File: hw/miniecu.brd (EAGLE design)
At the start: 50 x 50 mm, 60 parts

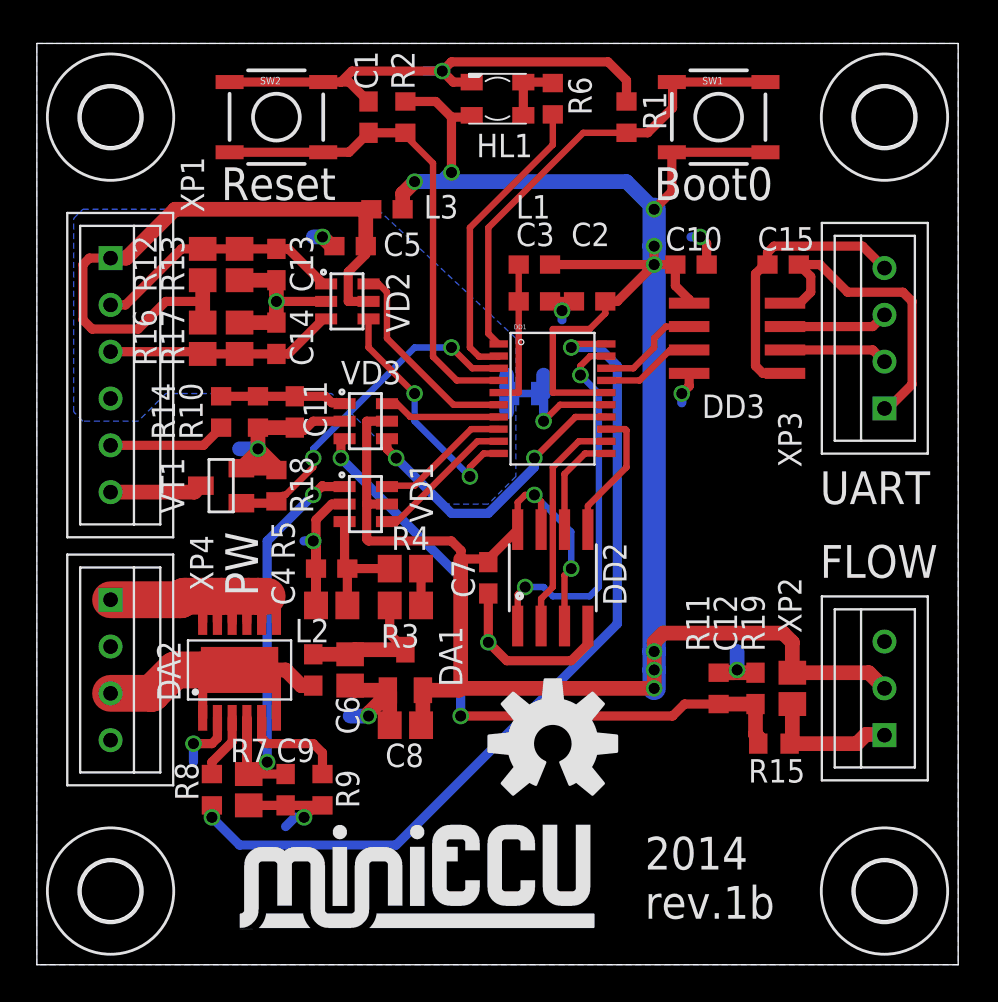
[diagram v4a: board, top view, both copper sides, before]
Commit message: hw: release v1c & update gerbers
changes from v1b:

- Use rounded corners.
- Add one GND drill.
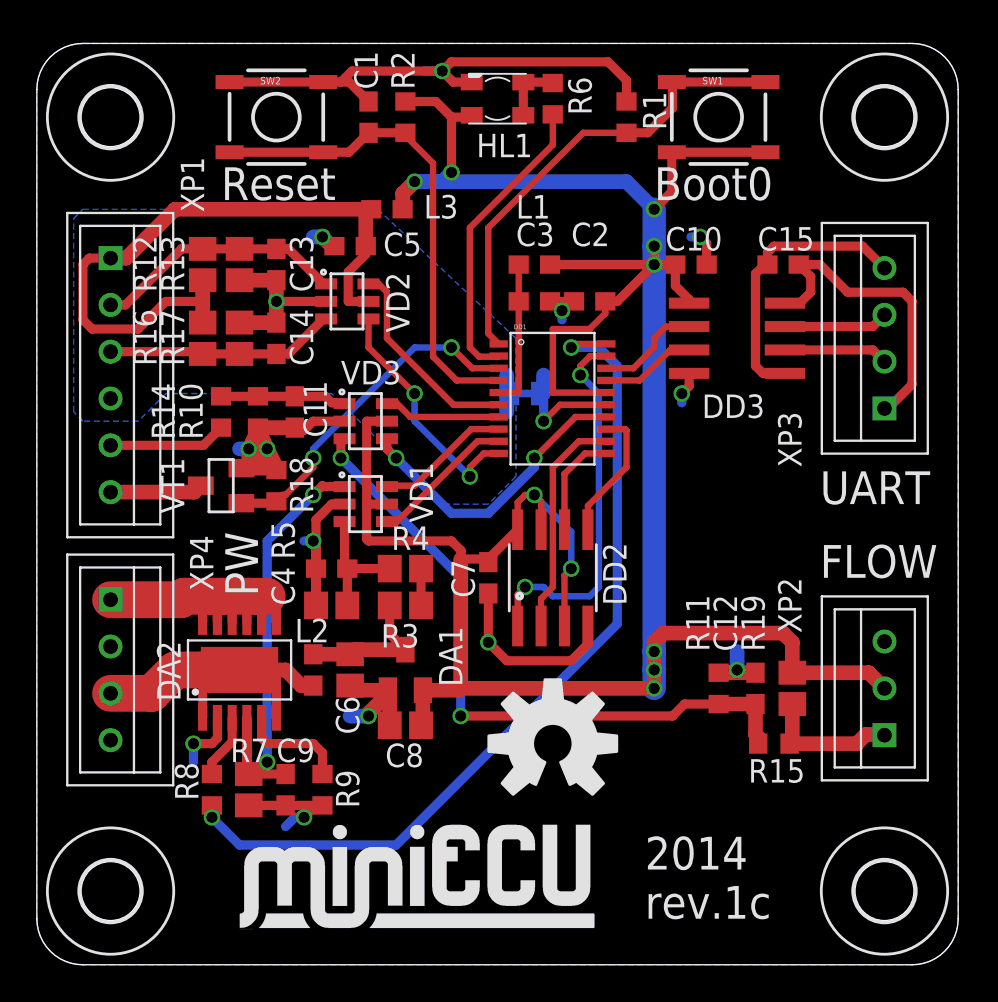
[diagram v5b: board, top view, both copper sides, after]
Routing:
- net GND: track 94.8 -> 98.6 mm, vias 12 -> 13
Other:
- outline, holes or cut-outs redrawn
- board text added: "2014 rev.1c"
- board text added: "miniECU rev.1c engine monitoring with kill switch"
- board text removed: "2014 rev.1b"
- board text removed: "miniECU rev.1b engine monitoring with kill switch"
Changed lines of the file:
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@@
 <board>
 <plain>
-<wire x1="0" y1="0" x2="50" y2="0" width="0" layer="20"/>
-<wire x1="50" y1="0" x2="50" y2="50" width="0" layer="20"/>
-<wire x1="50" y1="50" x2="0" y2="50" width="0" layer="20"/>
-<wire x1="0" y1="50" x2="0" y2="0" width="0" layer="20"/>
+<wire x1="0" y1="2.5" x2="2.5" y2="0" width="0" layer="20" curve="90"/>
+<wire x1="2.5" y1="0" x2="47.5" y2="0" width="0" layer="20"/>
+<wire x1="47.5" y1="0" x2="50" y2="2.5" width="0" layer="20" curve="90"/>
+<wire x1="50" y1="2.5" x2="50" y2="47.5" width="0" layer="20"/>
+<wire x1="50" y1="47.5" x2="47.5" y2="50" width="0" layer="20" curve="90"/>
+<wire x1="47.5" y1="50" x2="2.5" y2="50" width="0" layer="20"/>
+<wire x1="2.5" y1="50" x2="0" y2="47.5" width="0" layer="20" curve="90"/>
+<wire x1="0" y1="47.5" x2="0" y2="2.5" width="0" layer="20"/>
 <polygon width="0.5" layer="42">
 <vertex x="50" y="28"/>
@@
 </polygon>
 <text x="33" y="2.5" size="1.778" layer="21" font="vector">2014
-rev.1b</text>
+rev.1c</text>
 <text x="42.5" y="25" size="1.778" layer="21" font="vector">UART</text>
 <text x="42.5" y="21" size="1.778" layer="21" font="vector">FLOW</text>
@@
 <text x="35" y="31.75" size="2" layer="22" font="vector" rot="MR0" align="bottom-right">TXD</text>
 <text x="35" y="29.25" size="2" layer="22" font="vector" rot="MR0" align="bottom-right">VCCi</text>
-<text x="10.5" y="9.5" size="2" layer="22" font="fixed" rot="MR180">miniECU rev.1b
+<text x="10.5" y="9.5" size="2" layer="22" font="fixed" rot="MR180">miniECU rev.1c
 engine monitoring
 with kill switch</text>
@@
 <contactref element="HL1" pad="1"/>
 <polygon width="0.5" layer="16" isolate="0.254" rank="2">
-<vertex x="0" y="50"/>
-<vertex x="50" y="50"/>
-<vertex x="50" y="0"/>
-<vertex x="0" y="0"/>
+<vertex x="2.5" y="50"/>
+<vertex x="47.5" y="50" curve="-90"/>
+<vertex x="50" y="47.5"/>
+<vertex x="50" y="2.5" curve="-90"/>
+<vertex x="47.5" y="0"/>
+<vertex x="2.5" y="0" curve="-90"/>
+<vertex x="0" y="2.5"/>
+<vertex x="0" y="47.5" curve="-90"/>
 </polygon>
 <contactref element="R1" pad="1"/>
 <contactref element="SW2" pad="1"/>
 <wire x1="14.15" y1="29" x2="14" y2="29.15" width="0.5" layer="1"/>
-<wire x1="12" y1="29.15" x2="12" y2="28" width="0.8" layer="1"/>
-<wire x1="12" y1="28" x2="12" y2="27.85" width="0.8" layer="1"/>
-<wire x1="12" y1="27.85" x2="11.1" y2="26.95" width="0.8" layer="1"/>
+<wire x1="12" y1="29.15" x2="12.5" y2="28" width="0.8" layer="1"/>
 <wire x1="11.1" y1="26.95" x2="12.9" y2="26.95" width="0.8" layer="1"/>
 <wire x1="12.9" y1="26.95" x2="13" y2="26.85" width="0.8" layer="1"/>
 <wire x1="12" y1="29.15" x2="14" y2="29.15" width="0.8" layer="1"/>
 <wire x1="13" y1="26.85" x2="13" y2="27" width="0.8" layer="1"/>
-<wire x1="13" y1="27" x2="12" y2="28" width="0.8" layer="1"/>
-<via x="12" y="28" extent="1-16" drill="0.6"/>
-<wire x1="12" y1="28" x2="11" y2="28" width="0.8" layer="16"/>
+<wire x1="13" y1="27" x2="12.5" y2="28" width="0.8" layer="1"/>
+<via x="12.5" y="28" extent="1-16" drill="0.6"/>
+<wire x1="12.5" y1="28" x2="11" y2="28" width="0.8" layer="16"/>
 <wire x1="19.15" y1="13" x2="19.15" y2="14.8" width="0.8" layer="1"/>
 <wire x1="19.15" y1="14.8" x2="19.05" y2="14.9" width="0.8" layer="1"/>
@@
 <wire x1="27.5" y1="30.635" x2="27.135" y2="31" width="0.5" layer="16"/>
 <wire x1="27.5" y1="31" x2="27.5" y2="32" width="0.8" layer="16"/>
+<via x="11.5" y="28" extent="1-16" drill="0.6"/>
+<wire x1="11.5" y1="28" x2="11.5" y2="27" width="0.8" layer="1"/>
+<wire x1="11.5" y1="28" x2="12" y2="29" width="0.8" layer="1"/>
+<wire x1="11.5" y1="28" x2="12.5" y2="28" width="0.8" layer="1"/>
+<wire x1="11.5" y1="28" x2="13" y2="27" width="0.8" layer="1"/>
 <wire x1="27.135" y1="31" x2="27.5" y2="31" width="0" layer="19" extent="16-16"/>
 </signal>

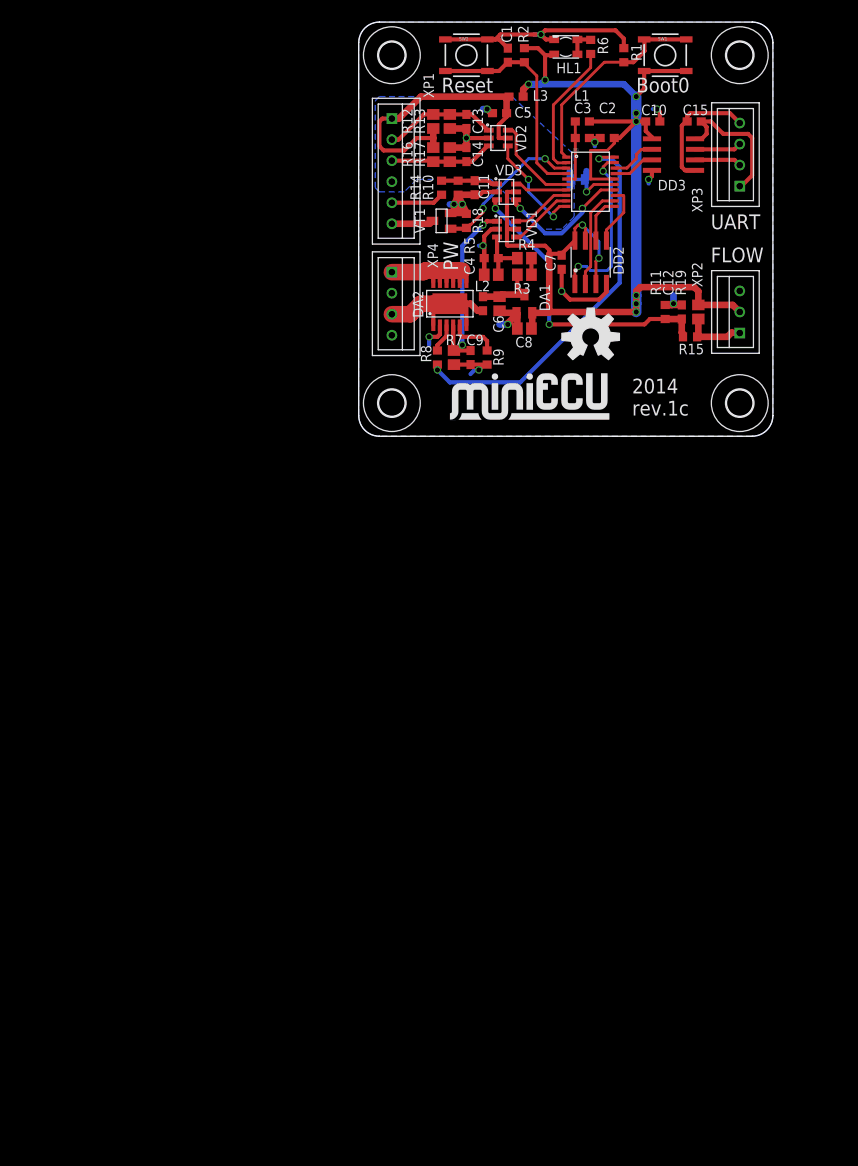
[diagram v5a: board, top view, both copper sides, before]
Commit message: hw: replace mcu
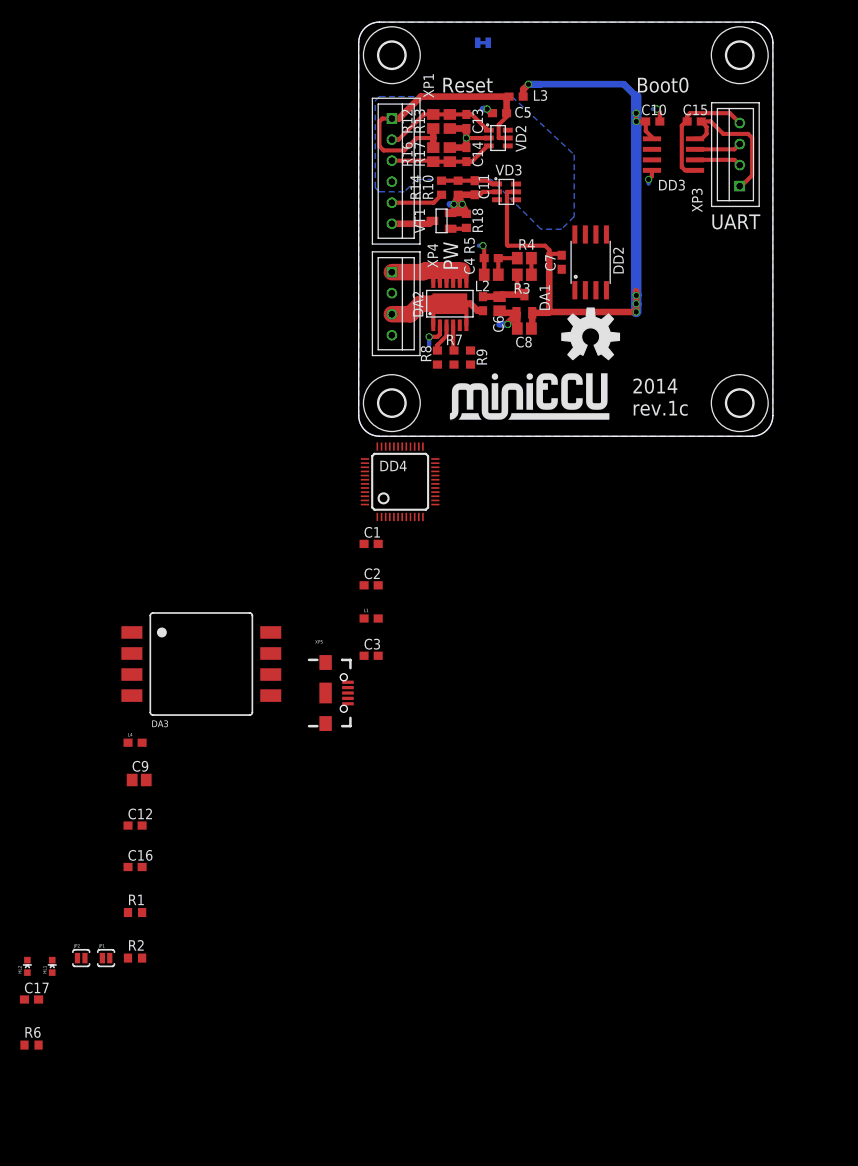
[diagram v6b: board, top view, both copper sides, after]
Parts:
- removed DD1: STM32F050F, stm32f050:TSSOP20
- removed R11: np, resistor:R0603
- removed R15: 140, resistor:R0603
- removed R19: 10k 1%, resistor:R0805
- removed SW1, SW2: (no value), SparkFun-Electromechanical:TACTILE_SWITCH_SMD
- removed VD1: USBLC6-2L, usblc6:SOT-23-6L
- removed XP2: B3B-XH-A, miniecu-con:B3B-XH
- added C16: 0.33, resistor:C0603
- added C17: 0.1, resistor:C0603
- added DA3: MP3V5004DP, microbuilder:SOP8-1351
- added DD4: STM32F373C, stm32f373:LQFP48
- added HL2: RED, SparkFun-LED:LED-0603
- added JP1, JP2: (no value), SparkFun-Passives:SJ_2S-NO
- added L4: FB, SparkFun-Passives:0603
- added XP5: USB_MICROB_PLUGCONN-11752, SparkFun-Connectors:USB-B-MICRO-SMD_V03
- C1: value 0.022 -> 0.1
- C12: value 0.022 -> 0.01
- C9: value 0.1 -> 1.0; device resistor:C0603 -> resistor:C0805
- DD2: value SPI_FLASH-X25XXSMD -> SPI_FLASH-X25XXSMD1; device SparkFun-DigitalIC:SO08 -> SparkFun-DigitalIC:SO08-EIAJ
- HL1: value KAA-3528ESGC -> GREEN; device led2:KA-3528 -> SparkFun-LED:LED-0603
- R1: value 5.1k -> 750
- R10: value np -> 10k
- R14, R6: value 140 -> 10k
- R18, R2, R9: value 5.1k -> 10k
- R7: value 10k 1% -> 1k; device resistor:R0805 -> resistor:R0603
- moved R6 138.1 mm to (-39.5, -73.5), turned to 0 degrees
- moved HL1 127.1 mm to (-37.0, -64.0), turned to 0 degrees
- moved R1 119.1 mm to (-27.0, -57.5), turned to 0 degrees
- moved R2 118.7 mm to (-27.0, -63.0), turned to 0 degrees
- moved C12 90.6 mm to (-27.0, -47.0), turned to 0 degrees
- moved C3 67.5 mm to (1.50, -26.5)
- moved L1 65.2 mm to (1.50, -22.0)
- moved C9 64.8 mm to (-26.5, -41.5), turned to 0 degrees
- moved C1 61.3 mm to (1.50, -13.0), turned to 0 degrees
- moved C2 61.1 mm to (1.50, -18.0), turned to 0 degrees
- moved PT1 20.1 mm to (15.0, 47.5)
- moved R9 2.00 mm to (13.5, 9.50)
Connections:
- removed net !NRST: C1.1, DD1.4, R2.1, SW2.3, SW2.4
- removed net AVCC: C3.1, DD1.5, L1.1
- removed net BOOT0: DD1.1, R1.2, SW1.1, SW1.2
- removed net FLOW_PULSE: C12.1, DD1.14, R11.2, R15.1, VD3.3, VD3.4
- removed net I_SENSE: C9.1, DA2.4, DD1.8, R7.1, VD1.1, VD1.6
- removed net LED: DD1.2, R6.1
- new net BAT: DD4.1
- new net FLOW: C16.1, R1.1
- new net N$10: C17.1, DD4.7, JP2.2
- new net N$11: DD4.44, JP1.1, R6.2
- new net N$3: C12.1, C9.1, DA3.2, L4.1
- new net N$5: C2.1, DD4.24, DD4.25, DD4.9, L1.1
- new net USB_DM: XP5.D-1
- new net USB_DP: XP5.D+1
- new net USB_VBUS: XP5.VBUS1
- net +3V3: now also C1.1, C3.1, DD4.17, DD4.48, JP1.2, L4.2; no longer C2.1, DD1.16, HL1.4, R19.2, R2.2, SW1.3, SW1.4, VD1.5, XP2.2
- net AGND: now also C2.2, DD4.23, DD4.8
- net FLASH_CS: no longer DD1.19
- net GND: now also C16.2, C17.2, DA3.3, DD4.47, JP2.1, R2.1, R6.1, XP5.GND1; no longer C2.2, DD1.15, HL1.1, R1.1, R11.1, SW2.1, SW2.2, VD1.2, XP2.3
- net IGN_EN: no longer DD1.20
- net MISO: no longer DD1.12
- net MOSI: no longer DD1.13
- net N$2: now also DA2.4, R7.1; no longer HL1.2, HL1.3, R6.2
- net N$4: now also DA3.4, R1.2; no longer R15.2, R19.1, XP2.1
- net OIL_PRES: no longer DD1.10
- net RPM_IN: now also R2.2; no longer DD1.7
- net RXD: no longer DD1.18
- net SCK: no longer DD1.11
- net STARTER: no longer DD1.3
- net THERM: no longer DD1.6
- net TXD: no longer DD1.17
- net V_SENSE: now also VD3.3, VD3.4; no longer DD1.9, VD1.3, VD1.4
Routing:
- net +3V3: track 153.1 -> 87.2 mm, vias 10 -> 6
- net GND: track 98.6 -> 36.4 mm, vias 13 -> 7
- net FLOW_PULSE: track 52.7 -> 0.00 mm, vias 4 -> 0
- net IGN_EN: track 47.1 -> 0.00 mm, vias 2 -> 0
- net I_SENSE: track 34.1 -> 0.00 mm, vias 2 -> 0
- net !NRST: track 26.8 -> 0.00 mm
- net BOOT0: track 25.7 -> 0.00 mm
- net FLASH_CS: track 20.7 -> 0.00 mm, vias 2 -> 0
- net STARTER: track 18.5 -> 1.94 mm, vias 2 -> 0
- net LED: track 16.3 -> 0.00 mm
- net OIL_PRES: track 25.7 -> 12.5 mm, vias 2 -> 0
- net MISO: track 12.4 -> 0.00 mm
- net THERM: track 25.0 -> 13.7 mm
- net V_SENSE: track 14.8 -> 4.51 mm
- net AVCC: track 8.04 -> 0.00 mm
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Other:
- board text removed: "+3.3"
- board text removed: "FLOW"
- board text removed: "GND"
- board text removed: "PULSE"

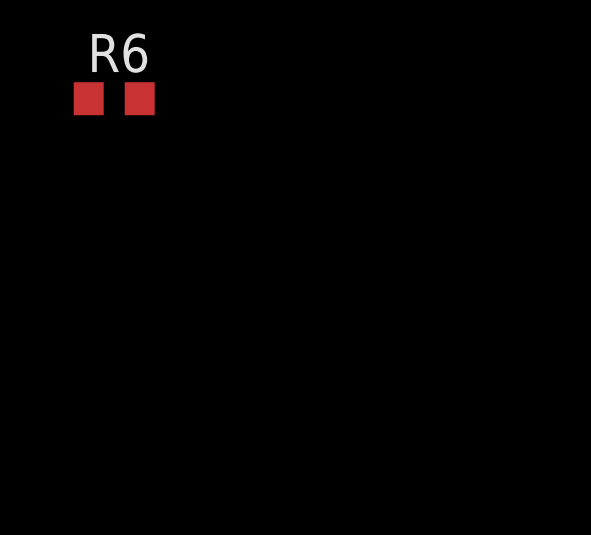
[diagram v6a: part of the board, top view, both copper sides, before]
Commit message: hw: add library for Murata CSTCE resonators
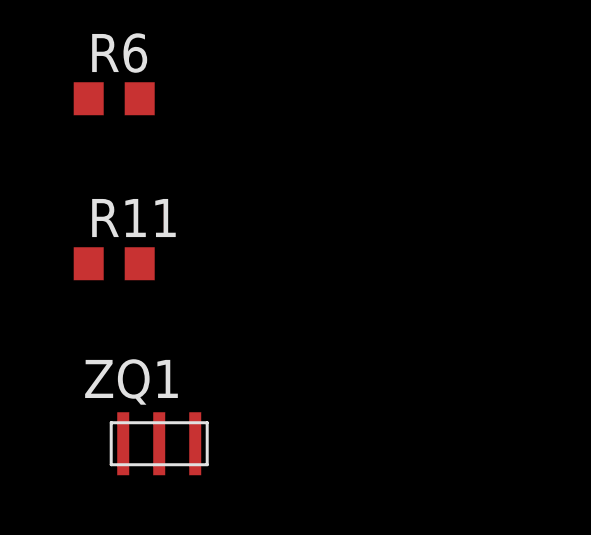
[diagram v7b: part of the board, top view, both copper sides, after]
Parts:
- added R11: 1.5k, resistor:R0603
- added ZQ1: CSTCE8M00G52-R0, cstce-resonator:CSTCE
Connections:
- new net OSC_IN: DD4.5, ZQ1.1
- new net OSC_OUT: DD4.6, ZQ1.3
- net GND: now also ZQ1.2
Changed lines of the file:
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@@
 <element name="C17" library="resistor" package="C0603" value="0.1" x="-39.5" y="-68"/>
 <element name="R6" library="resistor" package="R0603" value="10k" x="-39.5" y="-73.5"/>
+<element name="R11" library="resistor" package="R0603" value="1.5k" x="-39.5" y="-79"/>
+<element name="ZQ1" library="cstce-resonator" package="CSTCE" value="CSTCE8M00G52-R0" x="-38" y="-85">
+<attribute name="OC_MOUSER" value="81-CSTCE8M00G52-R0" x="-38" y="-85" size="1.778" layer="27" display="off"/>
+<attribute name="FREQUENCY" value="8 MHz" x="-38" y="-85" size="1.778" layer="27" display="off"/>
+</element>
 </elements>
 <signals>
@@
 <contactref element="R6" pad="1"/>
 <contactref element="C17" pad="2"/>
+<contactref element="ZQ1" pad="2"/>
+<wire x1="-40.35" y1="-73.5" x2="-38" y2="-85" width="0" layer="19" extent="1-1"/>
 <wire x1="-38.65" y1="-68" x2="-40.35" y2="-73.5" width="0" layer="19" extent="1-1"/>
 <wire x1="-33.95" y1="-63" x2="-38.65" y2="-68" width="0" layer="19" extent="1-1"/>
@@
 <wire x1="0.75" y1="-6.25" x2="-30.95" y2="-63" width="0" layer="19" extent="1-1"/>
 </signal>
+<signal name="OSC_OUT">
+<contactref element="DD4" pad="6"/>
+<contactref element="ZQ1" pad="3"/>
+<wire x1="4.75" y1="-9.75" x2="-36.8" y2="-85" width="0" layer="19" extent="1-1"/>
+</signal>
+<signal name="OSC_IN">
+<contactref element="DD4" pad="5"/>
+<contactref element="ZQ1" pad="1"/>
+<wire x1="4.25" y1="-9.75" x2="-39.2" y2="-85" width="0" layer="19" extent="1-1"/>
+</signal>
 </signals>
